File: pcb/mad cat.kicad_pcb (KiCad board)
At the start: 2 copper layers, 361.9 x 143 mm, 274 parts, among them J1 Conn_01x04, J2 Conn_02x03_Odd_Even, SW0,0 ESC, SW0,1 ESC/F1, SW0,10 F9, SW0,10-1 F10, SW0,11 F10, SW0,11-1 F11, SW0,12 F11, SW0,12-1 F12, SW0,13 F12/PRT, SW0,14 INS, SW0,15 HOME, SW0,16 PGUP, SW0,2 F1, SW0,2-1 F2, SW0,3 F2, SW0,3-1 F3, SW0,4 F3, SW0,4-1 F4, SW0,5 F4, SW0,5-1 F5, SW0,6 F5, SW0,6-1 F6, SW0,7 F6, SW0,7-1 F7, SW0,8 F7, SW0,8-1 F8, SW0,9 F8, SW0,9-1 F9, SW1,0 PF1, SW1,0-1 PF1, SW1,1 TILDE, SW1,10 9, SW1,11 0, SW1,12 -, SW1,13 =, SW1,14 BACKSPACE, SW1,14-1 S_BS_L, SW1,15 END, SW1,16 PGDN, SW1,2 1, SW1,3 2, SW1,4 3, SW1,5 4, SW1,6 5, SW1,7 6, SW1,8 7, SW1,9 8, SW2,0 PF2, SW2,0-1 PF2, SW2,1 TAB, SW2,10 O, SW2,11 P, SW2,12 [, SW2,13 ], SW2,14 \, SW2,15 S_BS_R, SW2,16 PRT, SW2,2 Q, SW2,3 W, SW2,4 E, SW2,5 R, SW2,6 T, SW2,7 Y, SW2,8 U, SW2,9 I, SW3,0 PF3, SW3,0-1 PF3, SW3,1 CAPS, SW3,1-1 ST_CAPS, SW3,10 L, SW3,11 COLONS, SW3,12 QUOTE, SW3,13 ISO_#, SW3,14 ENT, SW3,14-1 ISO_ENT, SW3,15 DEL, SW3,15-1 DEL, SW3,15-2 DEL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

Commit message: via stitch, proto diode footprint
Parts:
- D1, D10, D11, D12, D13, D14, D15, D16, D17, D18, D19, D2, D20, D21, D22, D23, D24, D25, D26, D27, D28, D29, D3, D30, D31, D32, D33, D34, D35, D36, D37, D38, D39, D4, D40, D41, D42, D43, D44, D45, D46, D47, D48, D49, D5, D50, D51, D52, D53, D54, D55, D56, D57, D58, D59, D6, D60, D61, D62, D63, D64, D65, D66, D67, D68, D69, D7, D70, D71, D72, D73, D74, D75, D76, D77, D78, D79, D8, D80, D81, D82, D83, D84, D85, D86, D87, D88, D89, D9, D90, D91, D92, D93, D94, D95, D96: footprint Diode_SMD:D_SOD-123 -> keebs:D_SOD-123proto
- moved G*** 0.12 mm to (202.0, 111.0) (x2)
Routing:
- net Net-(R5-Pad2): track 265.9 -> 263.7 mm
- net GND: vias 74 -> 6060
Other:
- board text added: "Timber Wolf proto by Crokto"

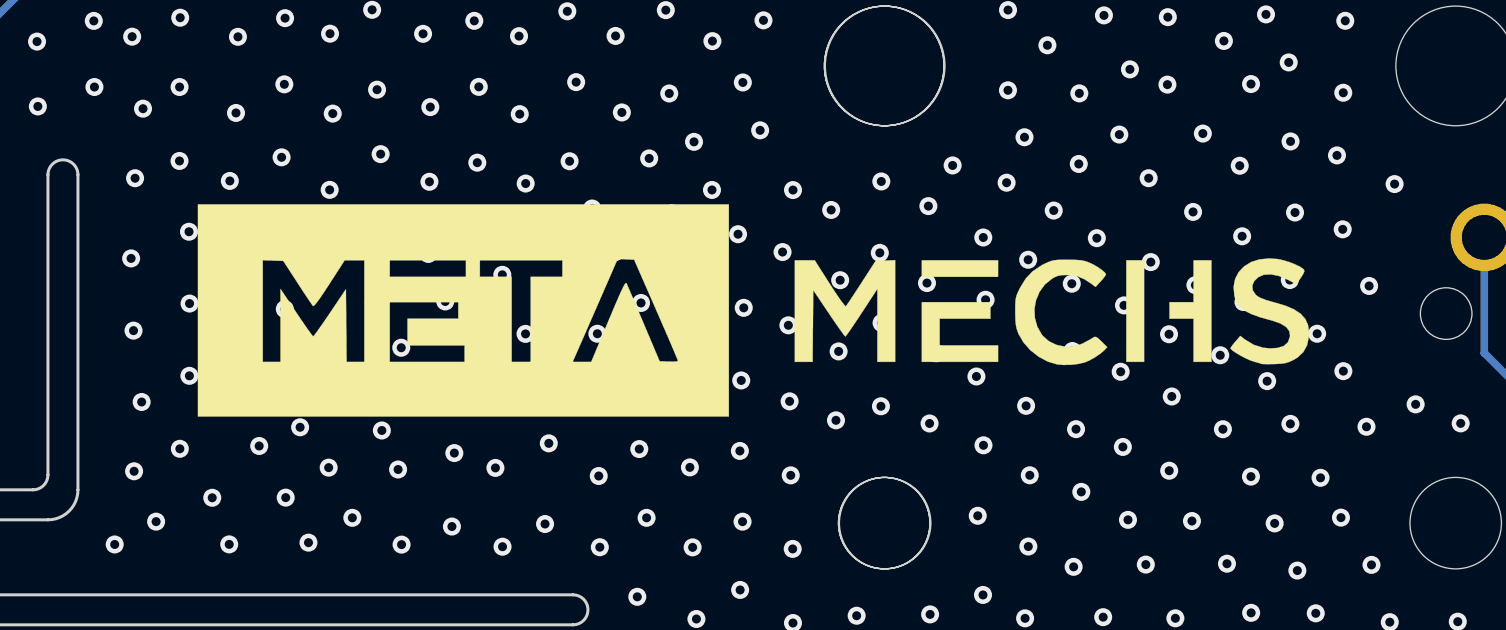
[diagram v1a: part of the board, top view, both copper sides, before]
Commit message: rremoved vias around logo
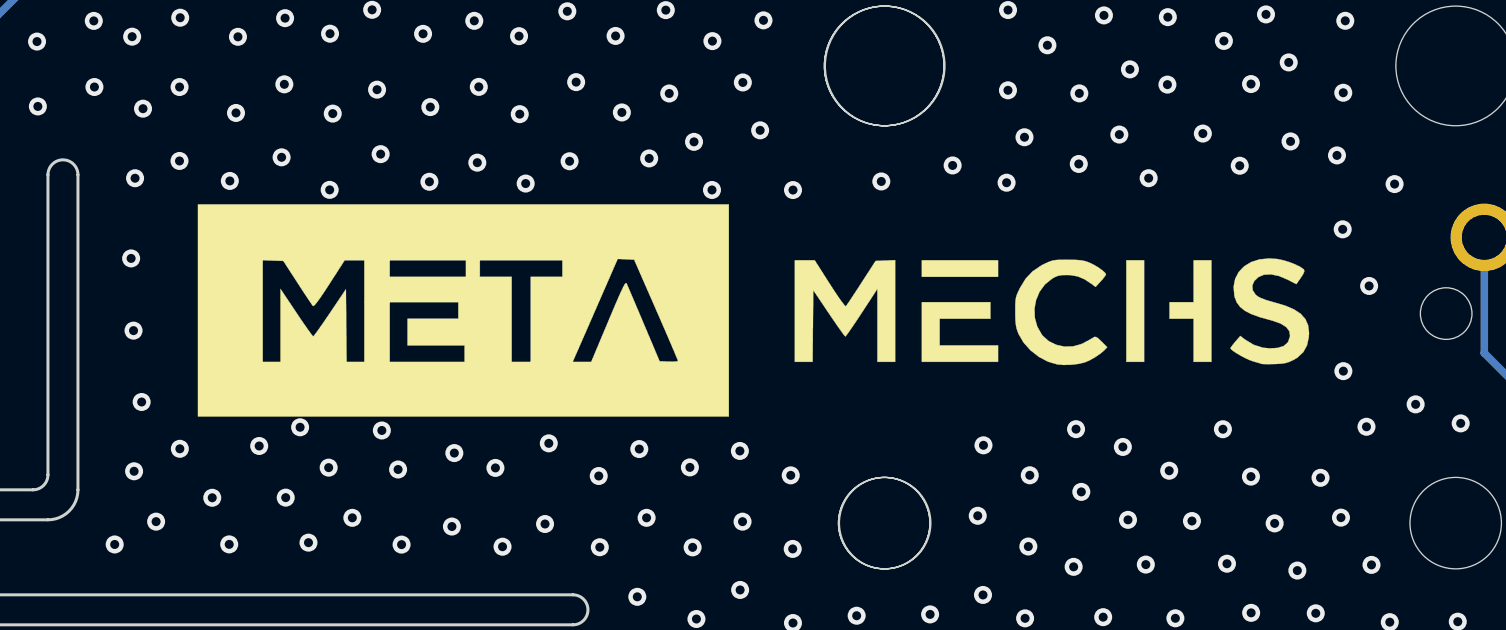
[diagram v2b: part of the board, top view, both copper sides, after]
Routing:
- net GND: vias 6060 -> 5982

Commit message: sent red proto to jlc
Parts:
- D1, D10, D11, D12, D13, D14, D15, D16, D17, D18, D19, D2, D20, D21, D22, D23, D24, D25, D26, D27, D28, D29, D3, D30, D31, D32, D33, D34, D35, D36, D37, D38, D39, D4, D40, D41, D42, D43, D44, D45, D46, D47, D48, D49, D5, D50, D51, D52, D53, D54, D55, D56, D57, D58, D59, D6, D60, D61, D62, D63, D64, D65, D66, D67, D68, D69, D7, D70, D71, D72, D73, D74, D75, D76, D77, D78, D79, D8, D80, D81, D82, D83, D84, D85, D86, D87, D88, D89, D9, D90, D91, D92, D93, D94, D95, D96: footprint keebs:D_SOD-123proto -> Diode_SMD:D_SOD-123
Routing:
- net GND: vias 5982 -> 83

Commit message: redo layout after ic
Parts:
- removed EC2-1: EC11E, keebs:EC11E
- removed G*** (x2): LOGO, logo:metamechs logo half
- removed SW5,12-2: ALT, MX_SMK_2:MX_150
- removed SW5,13-1: LEFT, MX_SMK_2:MX_100
- added D97: D, Diode_SMD:D_SOD-123, B.Cu at (339.1, 124.5)
- added SW5,10: ALT, MX_SMK_2:MX_150, F.Cu at (230.2, 111.1)
- added SW5,11-1: CTRL, MX_SMK_2:MX_150, F.Cu at (258.8, 111.1)
- added SW5,11-2: ALT, MX_SMK_2:MX_150, F.Cu at (249.2, 111.1)
- added SW5,16-2: 1u_ent, MX_SMK_2:MX_100, F.Cu at (352.4, 111.1)
- SW3,15, SW3,15-1: footprint MX_SMK_2:MX_200 -> MX_SMK_2:MX_200_stabflip
- SW4,16-1: value Extra 1u -> extra_1u
- SW5,11: value ALT -> WIN; footprint MX_SMK_2:MX_150 -> MX_SMK_2:MX_100
- SW5,12: value WIN -> CTRL; footprint MX_SMK_2:MX_100 -> MX_SMK_2:MX_150
- SW5,12-1: value CTRL -> LEFT; footprint MX_SMK_2:MX_150 -> MX_SMK_2:MX_100
- SW5,13: value CTRL -> LEFT/DOWN; footprint MX_SMK_2:MX_150 -> MX_SMK_2:MX_100
- SW5,14: value LEFT/DOWN -> DOWN/RIGHT
- SW5,15: value DOWN/RIGHT -> 1u
- SW5,7: value 6 SPACE -> 6.25 SPACE; footprint MX_SMK_2:MX_600_stabflip -> MX_SMK_2:MX_625_stabflip
- SW5,7-1: value 6.25 SPACE -> 7 SPACE; footprint MX_SMK_2:MX_625_stabflip -> MX_SMK_2:MX_700_stabflip
- SW5,7-3: value 7 SPACE -> 6 SPACE; footprint MX_SMK_2:MX_700_stabflip -> MX_SMK_2:MX_100
- moved H5 378.8 mm to (357.9, -4.00)
- moved H9 161.4 mm to (269.5, 131.0)
- moved H6 88.5 mm to (4.00, 131.0)
- moved H7 88.5 mm to (92.5, 131.0)
- moved H8 88.5 mm to (181.0, 131.0)
- moved SW5,15 35.9 mm to (352.4, 92.1)
- moved SW5,12-1 30.8 mm to (288.9, 117.5)
- moved SW5,13 30.8 mm to (308.0, 117.5)
- moved SW5,11 23.8 mm to (254.0, 111.1)
- moved SW5,12 23.8 mm to (277.8, 111.1)
- moved SW3,16-1 19.0 mm to (352.4, 73.0)
- moved SW5,14 19.0 mm to (327.0, 117.5)
- moved D70 16.6 mm to (27.9, 99.1)
- moved D50 15.6 mm to (294.5, 42.1)
- moved D52 15.5 mm to (2.52, 80.0)
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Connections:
- D96 pad 1: /r5 -> Net-(D96-Pad1)
- SW5,11 pad 1: Net-(D91-Pad2) -> Net-(D92-Pad2)
- SW5,12 pad 1: Net-(D92-Pad2) -> Net-(D93-Pad2)
- SW5,12-1 pad 1: /c12 -> Net-(D93-Pad2)
- SW5,12-1 pad 2: Net-(D92-Pad2) -> /c12
- SW5,13 pad 1: Net-(D93-Pad2) -> Net-(D94-Pad2)
- SW5,14 pad 1: Net-(D94-Pad2) -> Net-(D95-Pad2)
- SW5,15 pad 1: Net-(D95-Pad2) -> Net-(D96-Pad2)
- SW5,16 pad 1: Net-(D96-Pad2) -> Net-(D97-Pad2)
- SW5,16-1 pad 1: Net-(D96-Pad2) -> Net-(D97-Pad2)
- SW5,7-1 pad 1: Net-(D90-Pad2) -> /c7
- SW5,7-1 pad 2: /c7 -> Net-(D90-Pad2)
- SW5,7-3 pad 1: /c7 -> Net-(D90-Pad2)
- SW5,7-3 pad 2: Net-(D90-Pad2) -> /c7
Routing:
- net /enc+: track 538.6 -> 0.00 mm, vias 4 -> 0
- net /enc-: track 501.4 -> 0.00 mm, vias 4 -> 0
- net /r0: track 455.2 -> 0.00 mm, vias 4 -> 0
- net /r1: track 413.7 -> 0.00 mm, vias 4 -> 0
- net /c16: track 407.8 -> 0.00 mm, vias 2 -> 0
- net /r5: track 406.0 -> 0.00 mm, vias 6 -> 0
- net /r3: track 399.2 -> 0.00 mm, vias 6 -> 0
- net /r2: track 395.9 -> 0.00 mm, vias 4 -> 0
- net /c15: track 382.8 -> 0.00 mm, vias 2 -> 0
- net /c13: track 362.8 -> 0.00 mm, vias 1 -> 0
- net /r4: track 359.7 -> 0.00 mm, vias 2 -> 0
- net /c14: track 347.5 -> 0.00 mm, vias 1 -> 0
- net VCC: track 297.5 -> 0.00 mm, vias 8 -> 0
- net /c1: track 295.6 -> 0.00 mm, vias 2 -> 0
- net /c12: track 284.1 -> 0.00 mm, vias 1 -> 0
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- removed copper zone on B.Cu, net GND
- removed copper zone on F.Cu, net GND
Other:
- board text removed: "Timber Wolf proto by Crokto"

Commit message: progress on redo
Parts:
- moved D96 27.0 mm to (345.4, 99.0), turned to 270 degrees
- moved D90 11.9 mm to (142.7, 114.7), turned to 0 degrees
- moved D94 5.10 mm to (300.0, 119.5)
- moved D95 5.10 mm to (319.0, 119.5)
- moved D97 5.10 mm to (338.1, 119.5)
- moved D87 3.54 mm to (30.2, 115.6)
- moved D89 2.64 mm to (80.0, 115.5)
- moved D88 2.62 mm to (56.5, 115.5)
- moved C10 0.50 mm to (8.70, 15.4)
- moved R7 0.50 mm to (8.00, 17.3)
- moved C12 0.20 mm to (351.0, 64.8)
- moved C13 0.20 mm to (350.0, 60.2)
- moved R10 0.20 mm to (348.0, 60.2)
- moved R9 0.20 mm to (349.0, 64.8)
- moved C5 0.10 mm to (116.4, 117.5)
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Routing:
- net /c16: track 0.00 -> 401.7 mm
- net /r2: track 0.00 -> 332.6 mm
- net /r1: track 0.00 -> 325.1 mm
- net /r0: track 0.00 -> 317.5 mm
- net /r4: track 0.00 -> 306.4 mm
- net /c1: track 0.00 -> 294.2 mm, vias 0 -> 1
- net /r3: track 0.00 -> 292.6 mm
- net GND: track 0.00 -> 282.4 mm, vias 0 -> 4
- net /c2: track 0.00 -> 276.9 mm, vias 0 -> 1
- net Net-(R5-Pad2): track 0.00 -> 276.4 mm, vias 0 -> 2
- net VCC: track 0.00 -> 260.7 mm, vias 0 -> 5
- net /enc+: track 0.00 -> 244.7 mm, vias 0 -> 2
- net /c0: track 0.00 -> 238.0 mm, vias 0 -> 1
- net /enc-: track 0.00 -> 225.2 mm, vias 0 -> 2
- net /RES: track 0.00 -> 215.5 mm, vias 0 -> 3
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- added copper zone on B.Cu, net GND
- added copper zone on F.Cu, net GND

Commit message: via stitched proto
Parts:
- added G***: LOGO, logo:metamechs logo half, B.Cu at (200.0, 110.5)
- D1, D10, D11, D12, D13, D14, D15, D16, D17, D18, D19, D2, D20, D21, D22, D23, D24, D25, D26, D27, D28, D29, D3, D30, D31, D32, D33, D34, D35, D36, D37, D38, D39, D4, D40, D41, D42, D43, D44, D45, D46, D47, D48, D49, D5, D50, D51, D52, D53, D54, D55, D56, D57, D58, D59, D6, D60, D61, D62, D63, D64, D65, D66, D67, D68, D69, D7, D70, D71, D72, D73, D74, D75, D76, D77, D78, D79, D8, D80, D81, D82, D83, D84, D85, D86, D87, D88, D89, D9, D90, D91, D92, D93, D94, D95, D96, D97: footprint Diode_SMD:D_SOD-123 -> keebs:D_SOD-123proto
- moved D86 15.7 mm to (17.5, 123.0)
- moved D18 15.1 mm to (17.5, 40.4)
- moved D35 15.1 mm to (17.5, 59.5)
- moved D52 15.1 mm to (17.5, 78.5)
- moved D69 15.1 mm to (17.5, 97.6)
- moved SW5,2-1 4.76 mm to (61.1, 111.1)
- moved SW5,3-1 4.76 mm to (84.9, 111.1)
- turned D96 to 0 degrees
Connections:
- D96 pad 1: Net-(D96-Pad1) -> /r5
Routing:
- net /enc+: track 244.7 -> 538.4 mm, vias 2 -> 4
- net /enc-: track 225.2 -> 517.0 mm, vias 2 -> 4
- net /c15: track 167.5 -> 426.1 mm, vias 0 -> 3
- net /r5: track 170.0 -> 419.0 mm, vias 0 -> 5
- net /c14: track 166.6 -> 387.7 mm, vias 0 -> 1
- net /c13: track 157.7 -> 356.3 mm, vias 0 -> 1
- net /c12: track 161.0 -> 339.0 mm, vias 0 -> 1
- net /c11: track 156.7 -> 292.7 mm, vias 0 -> 1
- net /r0: track 317.5 -> 446.5 mm, vias 0 -> 4
- net /c10: track 137.7 -> 262.8 mm, vias 0 -> 1
- net /r1: track 325.1 -> 409.5 mm, vias 0 -> 4
- net /r3: track 292.6 -> 376.9 mm, vias 0 -> 8
- net /c9: track 107.7 -> 190.3 mm, vias 0 -> 1
- net /r4: track 306.4 -> 378.9 mm, vias 0 -> 2
- net /r2: track 332.6 -> 402.0 mm, vias 0 -> 4
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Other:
- board text added: "Timber Wolf Proto by Crokto"
